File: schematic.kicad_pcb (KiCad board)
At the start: 2 copper layers, 169.7 x 127.8 mm, 116 parts, among them J3 USB_C_Receptacle_USB2.0_16P

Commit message: v1.0.0: Update title block, add project version variable
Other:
- board text added: "${VER}"
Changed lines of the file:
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@@
 			(plot_on_all_layers_selection 0x0000000_00000000)
 			(disableapertmacros no)
-			(usegerberextensions no)
+			(usegerberextensions yes)
 			(usegerberattributes yes)
 			(usegerberadvancedattributes yes)
@@
 			(outputformat 1)
 			(mirror no)
-			(drillshape 1)
+			(drillshape 0)
 			(scaleselection 1)
-			(outputdirectory "")
+			(outputdirectory "output/gerbers/")
 		)
 	)
+	(property "VER" "v1.0.0")
 	(net 0 "")
 	(net 1 "Net-(D1-A)")
@@
 		)
 	)
+	(gr_text "${VER}"
+		(at 104.5 186.25 354)
+		(layer "F.SilkS")
+		(effects
+			(font
+				(size 1 1)
+				(thickness 0.1524)
+				(bold yes)
+			)
+			(justify left bottom)
+		)
+	)

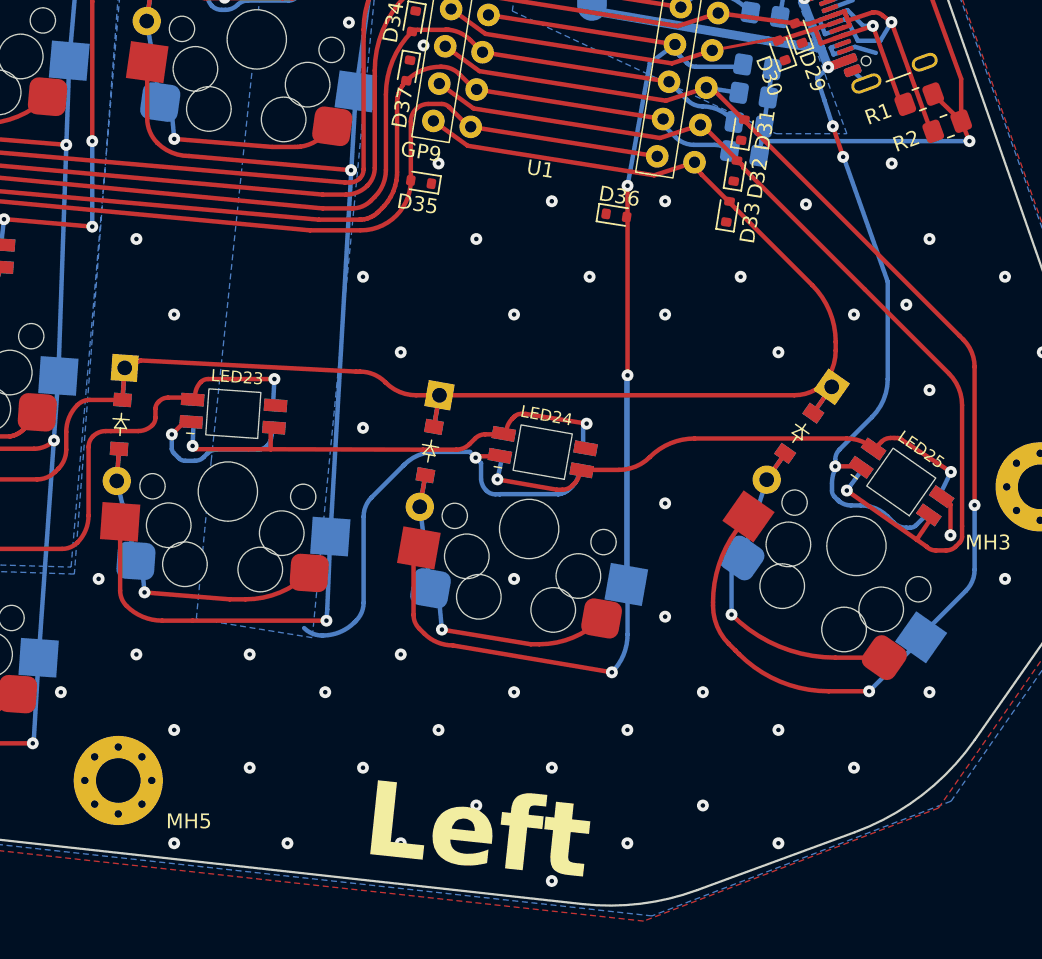
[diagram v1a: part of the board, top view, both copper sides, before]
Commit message: v1.1.0: Add stabilizers to 2u keys
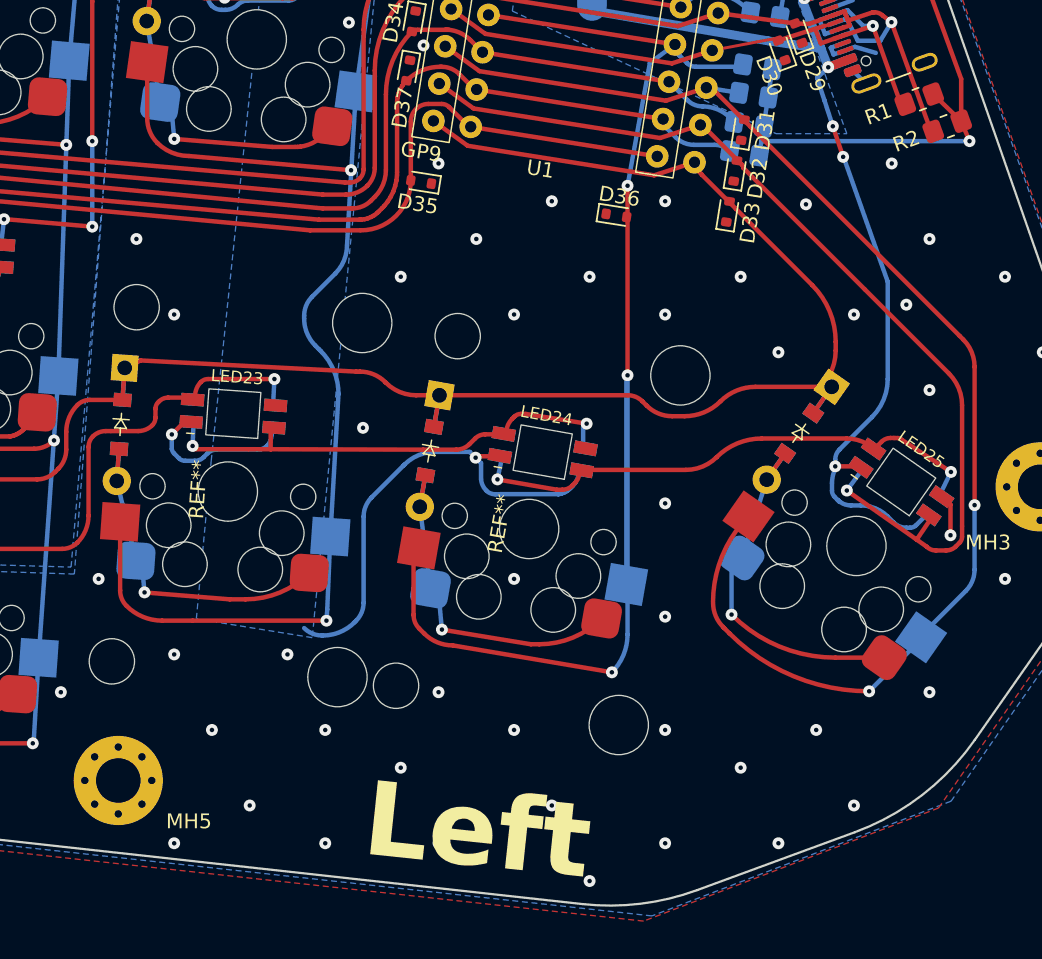
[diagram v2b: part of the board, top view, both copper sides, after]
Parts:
- added REF**: Stabilizer_Cherry_MX_2.00u, footprints:Stabilizer_Cherry_MX_2.00u, F.Cu at (173.4, 169.8)
- added REF**: Stabilizer_Cherry_MX_2.00u, footprints:Stabilizer_Cherry_MX_2.00u, F.Cu at (153.1, 167.3)
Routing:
- net /P1: track 183.4 -> 185.0 mm
- net /P9: track 151.3 -> 152.4 mm
- net /P7: track 92.1 -> 91.5 mm
- net GND: vias 167 -> 163
